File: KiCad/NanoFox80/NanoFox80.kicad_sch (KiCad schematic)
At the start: 59 parts, among them J101 Conn_01x02, J102 Conn_01x02, J103 Conn_01x02, J104 Conn_01x02, J111 DB9 Female, J112 Conn_01x02, J113 Conn_01x02, J115 Conn_01x02, P101 ISP/PDI, Q101 BSS84W-7-F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

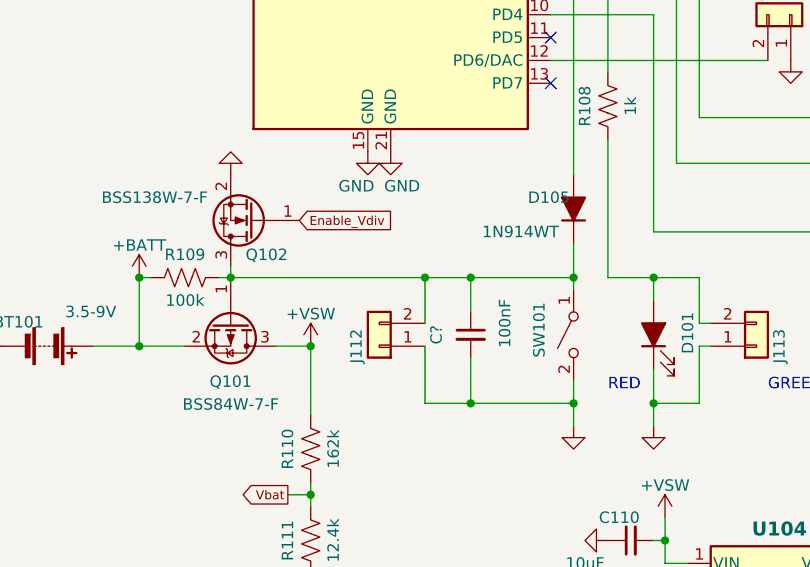
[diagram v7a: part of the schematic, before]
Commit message: Schematic Tweaks
Added missing diode
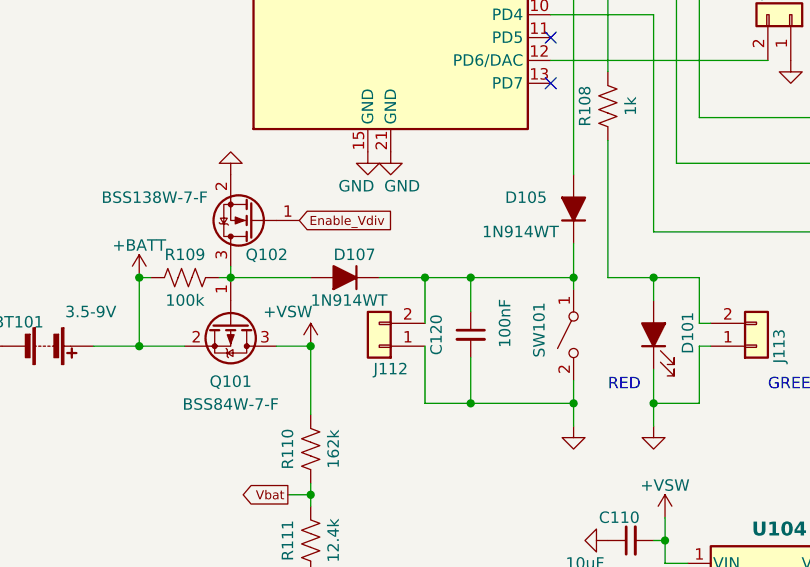
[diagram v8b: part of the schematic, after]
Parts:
- added D107: 1N914WT, Diode_SMD:D_SOD-523, symbol Diode:1N914WT
- gave numbers to parts that had none: 1
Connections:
- net at C120.1, D105.1 (K), J112.2 (Pin_2)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: now also D107.1 (K); no longer Q101.1 (G), Q102.3 (D), R109.2
- new net: D107.2 (A), Q101.1 (G), Q102.3 (D), R109.2
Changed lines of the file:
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@@
     (stroke (width 0) (type default) (color 0 0 0 0))
   )
-  (wire (pts (xy 41.91 151.13) (xy 63.5 151.13))
+  (wire (pts (xy 41.91 151.13) (xy 50.8 151.13))
     (stroke (width 0) (type default) (color 0 0 0 0))
   )
@@
     (stroke (width 0) (type default) (color 0 0 0 0))
   )
+  (wire (pts (xy 58.42 151.13) (xy 63.5 151.13))
+    (stroke (width 0) (type default) (color 0 0 0 0))
+  )
   (wire (pts (xy 31.75 101.6) (xy 31.75 104.14))
     (stroke (width 0) (type default) (color 0 0 0 0))
@@
     (pin "1")
   )
+  (symbol (lib_id "Diode:1N914WT") (at 54.61 151.13 180) (unit 1)
+    (in_bom yes) (on_board yes)
+    (property "Reference" "D107" (id 0) (at 53.34 148.59 0)
+      (effects (font (size 1.27 1.27)) (justify right))
+    )
+    (property "Value" "1N914WT" (id 1) (at 50.8 153.67 0)
+      (effects (font (size 1.27 1.27)) (justify right))
+    )
+    (property "Footprint" "Diode_SMD:D_SOD-523" (id 2) (at 54.61 146.685 0)
+      (effects (font (size 1.27 1.27)) hide)
+    )
+    (property "Datasheet" "http://www.mouser.com/ds/2/149/1N4148WT-461550.pdf" (id 3) (at 54.61 151.13 0)
+      (effects (font (size 1.27 1.27)) hide)
+    )
+    (pin "1")
+    (pin "2")
+  )
   (symbol (lib_id "Device:C_Trim_Small") (at 199.39 55.88 180) (unit 1)
     (in_bom yes) (on_board yes) (fields_autoplaced)
@@
   )
   (symbol (lib_id "power:+VSW") (at 50.8 158.75 0) (unit 1)
-    (in_bom yes) (on_board yes) (fields_autoplaced)
-    (property "Reference" "#PWR?" (id 0) (at 50.8 162.56 0)
+    (in_bom yes) (on_board yes)
+    (property "Reference" "#PWR0128" (id 0) (at 50.8 162.56 0)
       (effects (font (size 1.27 1.27)) hide)
     )
-    (property "Value" "+VSW" (id 1) (at 50.8 155.1742 0))
+    (property "Value" "+VSW" (id 1) (at 48.26 154.94 0))
     (property "Footprint" "" (id 2) (at 50.8 158.75 0)
       (effects (font (size 1.27 1.27)) hide)
@@
   (symbol (lib_id "Diode:1N914WT") (at 80.01 143.51 90) (unit 1)
     (in_bom yes) (on_board yes)
-    (property "Reference" "D105" (id 0) (at 74.93 142.24 90)
+    (property "Reference" "D105" (id 0) (at 72.39 142.24 90)
       (effects (font (size 1.27 1.27)) (justify right))
     )
@@
   (symbol (lib_id "Device:C_Small") (at 68.58 157.48 0) (unit 1)
     (in_bom yes) (on_board yes)
-    (property "Reference" "C?" (id 0) (at 64.77 157.48 90))
+    (property "Reference" "C120" (id 0) (at 64.77 157.48 90))
     (property "Value" "100nF" (id 1) (at 72.39 156.21 90))
     (property "Footprint" "Capacitor_SMD:C_0805_2012Metric_Pad1.18x1.45mm_HandSolder" (id 2) (at 68.58 157.48 0)
@@
   (symbol (lib_id "power:+VSW") (at 90.17 177.8 0) (unit 1)
     (in_bom yes) (on_board yes) (fields_autoplaced)
-    (property "Reference" "#PWR?" (id 0) (at 90.17 181.61 0)
+    (property "Reference" "#PWR0157" (id 0) (at 90.17 181.61 0)
       (effects (font (size 1.27 1.27)) hide)
     )
@@
   (symbol (lib_id "power:+VSW") (at 36.83 29.21 0) (unit 1)
     (in_bom yes) (on_board yes) (fields_autoplaced)
-    (property "Reference" "#PWR?" (id 0) (at 36.83 33.02 0)
+    (property "Reference" "#PWR0104" (id 0) (at 36.83 33.02 0)
       (effects (font (size 1.27 1.27)) hide)
     )
@@
   (symbol (lib_id "Connector_Generic:Conn_01x02") (at 58.42 158.75 180) (unit 1)
     (in_bom yes) (on_board yes)
-    (property "Reference" "J112" (id 0) (at 55.88 158.75 90))
+    (property "Reference" "J112" (id 0) (at 59.69 161.29 0))
     (property "Value" "Conn_01x02" (id 1) (at 58.42 161.1829 0)
       (effects (font (size 1.27 1.27)) hide)
@@
       (reference "#PWR0103") (unit 1) (value "GND") (footprint "")
     )
+    (path "/bd6b6d07-bcc0-4e70-87e3-edf6a5aca5a3"
+      (reference "#PWR0104") (unit 1) (value "+VSW") (footprint "")
+    )
     (path "/c932b361-059f-4797-bb48-55acd54d22ae"
       (reference "#PWR0105") (unit 1) (value "+3V3") (footprint "")
@@
       (reference "#PWR0127") (unit 1) (value "GND") (footprint "")
     )
+    (path "/402b505a-3134-4180-8252-3cb6368585af"
+      (reference "#PWR0128") (unit 1) (value "+VSW") (footprint "")
+    )
     (path "/4f7a1eba-8dbc-4c27-9d23-77ce339ae68b"
       (reference "#PWR0129") (unit 1) (value "VDD") (footprint "")
@@
       (reference "#PWR0156") (unit 1) (value "GND") (footprint "")
     )
+    (path "/a3e4e30c-206c-441f-ab18-6136621c1881"
+      (reference "#PWR0157") (unit 1) (value "+VSW") (footprint "")
+    )
     (path "/11e76ef2-618d-4ad6-8a58-2f677f10418e"
       (reference "#PWR0158") (unit 1) (value "GND") (footprint "")
@@
       (reference "#PWR0202") (unit 1) (value "GND") (footprint "")
     )
+    (path "/a6cf679a-8fe8-43b4-a04f-10097436e2b4/6fe5f251-d125-403e-ab6b-dbe26cac51a9"
+      (reference "#PWR0203") (unit 1) (value "+VSW") (footprint "")
+    )
     (path "/a6cf679a-8fe8-43b4-a04f-10097436e2b4/02034456-d704-450b-856e-6d640ab38367"
       (reference "#PWR0204") (unit 1) (value "GND") (footprint "")
@@
       (reference "#PWR0209") (unit 1) (value "GND") (footprint "")
     )
-    (path "/402b505a-3134-4180-8252-3cb6368585af"
-      (reference "#PWR?") (unit 1) (value "+VSW") (footprint "")
-    )
-    (path "/a6cf679a-8fe8-43b4-a04f-10097436e2b4/6fe5f251-d125-403e-ab6b-dbe26cac51a9"
-      (reference "#PWR?") (unit 1) (value "+VSW") (footprint "")
-    )
-    (path "/a3e4e30c-206c-441f-ab18-6136621c1881"
-      (reference "#PWR?") (unit 1) (value "+VSW") (footprint "")
-    )
-    (path "/bd6b6d07-bcc0-4e70-87e3-edf6a5aca5a3"
-      (reference "#PWR?") (unit 1) (value "+VSW") (footprint "")
-    )
     (path "/c938e709-b8e6-465b-a1ac-8390c5f3f4c9"
       (reference "AE101") (unit 1) (value "Antenna_Shield") (footprint "Connector_PinHeader_2.54mm:PinHeader_1x02_P2.54mm_Vertical")
@@
       (reference "C119") (unit 1) (value "TBD pF") (footprint "Capacitor_SMD:C_0805_2012Metric")
     )
+    (path "/6ff25e28-6290-4c29-a474-b6a86c1058fa"
+      (reference "C120") (unit 1) (value "100nF") (footprint "Capacitor_SMD:C_0805_2012Metric_Pad1.18x1.45mm_HandSolder")
+    )
     (path "/6acc6fcf-4b9f-4444-92c4-4fe7b9ec74a5"
       (reference "C121") (unit 1) (value "100nF") (footprint "Capacitor_SMD:C_0805_2012Metric_Pad1.18x1.45mm_HandSolder")
@@
       (reference "C203") (unit 1) (value "100nF") (footprint "Capacitor_SMD:C_0805_2012Metric_Pad1.18x1.45mm_HandSolder")
     )
-    (path "/6ff25e28-6290-4c29-a474-b6a86c1058fa"
-      (reference "C?") (unit 1) (value "100nF") (footprint "Capacitor_SMD:C_0805_2012Metric_Pad1.18x1.45mm_HandSolder")
-    )
     (path "/3d96634f-3b26-447f-8ede-f6059a78b14d"
       (reference "D101") (unit 1) (value "LED_Filled") (footprint "LED_SMD:LED_APDA1806SECK")
@@
       (reference "D106") (unit 1) (value "LED_Filled") (footprint "LED_SMD:LED_APDA1806SECK")
     )
+    (path "/0d0a8cf0-7e30-4463-a75a-b09ac9dce329"
+      (reference "D107") (unit 1) (value "1N914WT") (footprint "Diode_SMD:D_SOD-523")
+    )
     (path "/a27abb84-56e0-453a-b41b-2d099dd070cf"
